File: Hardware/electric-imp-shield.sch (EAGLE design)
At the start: 37 parts, among them Q2 BSS138, Q3 BSS138, U1 ELECTRIC_IMP, U2 ARDUINO_SHIELD, U3 MIC5219-3.3, U4 ATSHA204-TSU

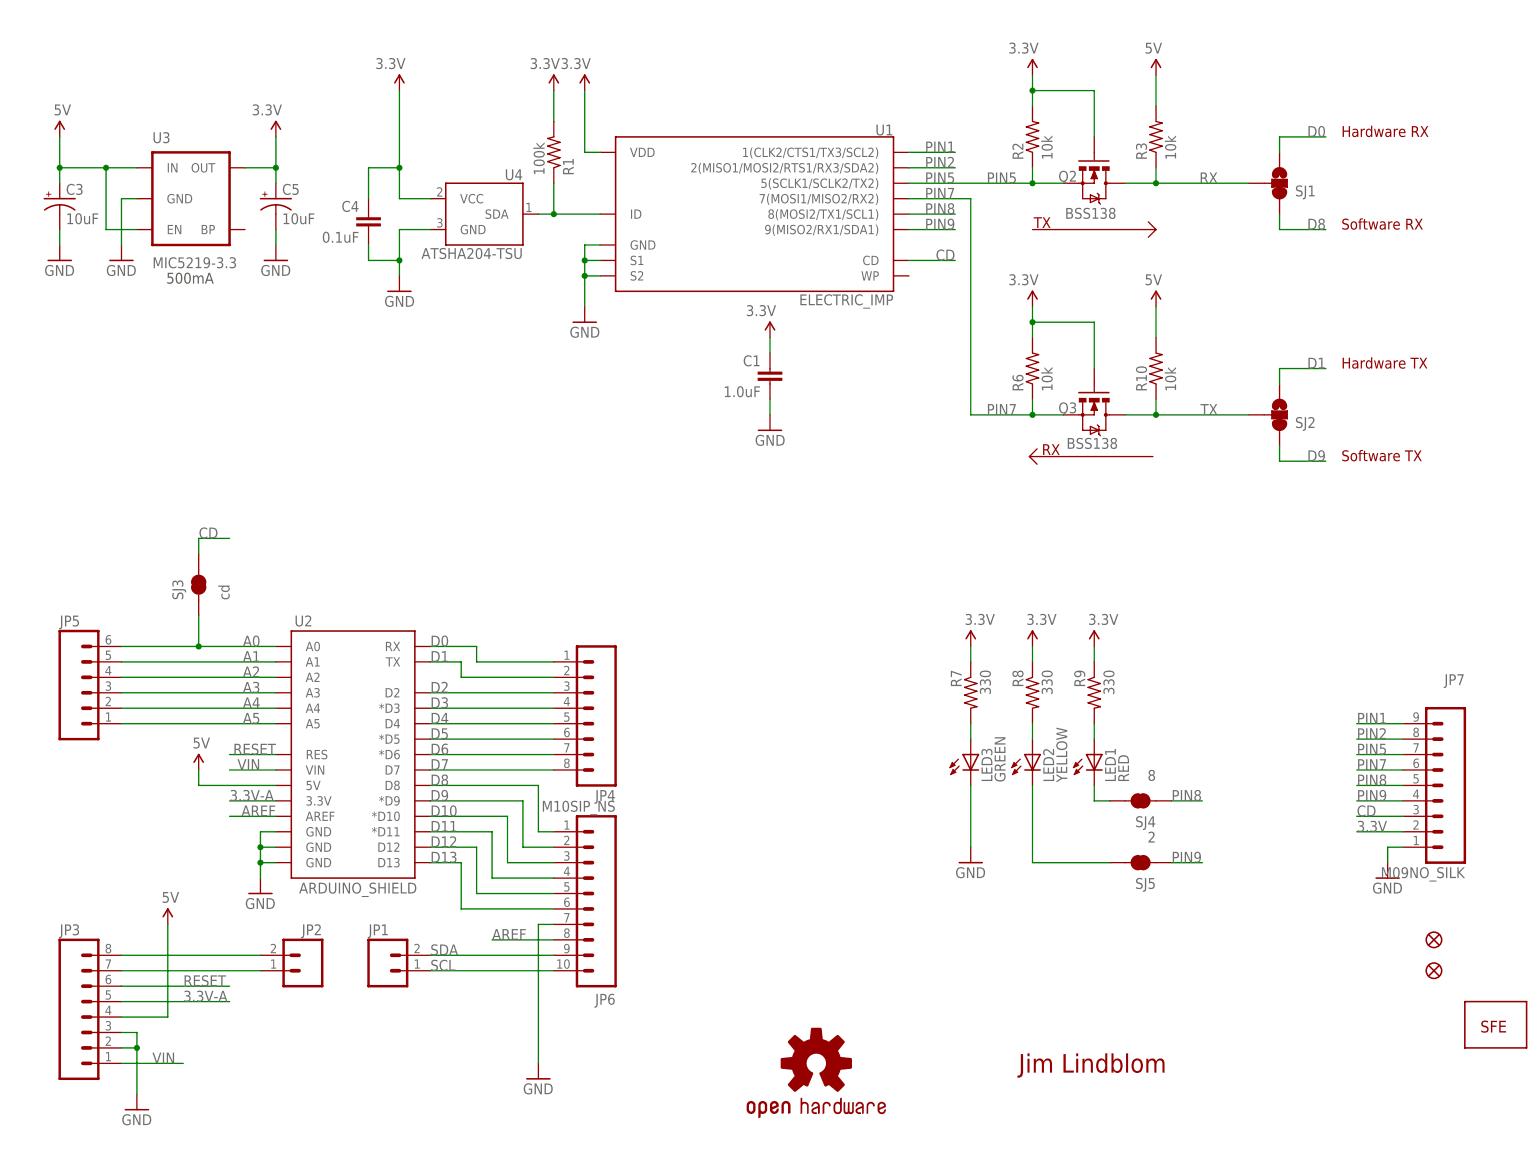
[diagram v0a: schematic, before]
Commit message: Updating to new socket fp, 0603 packages, schematic updates
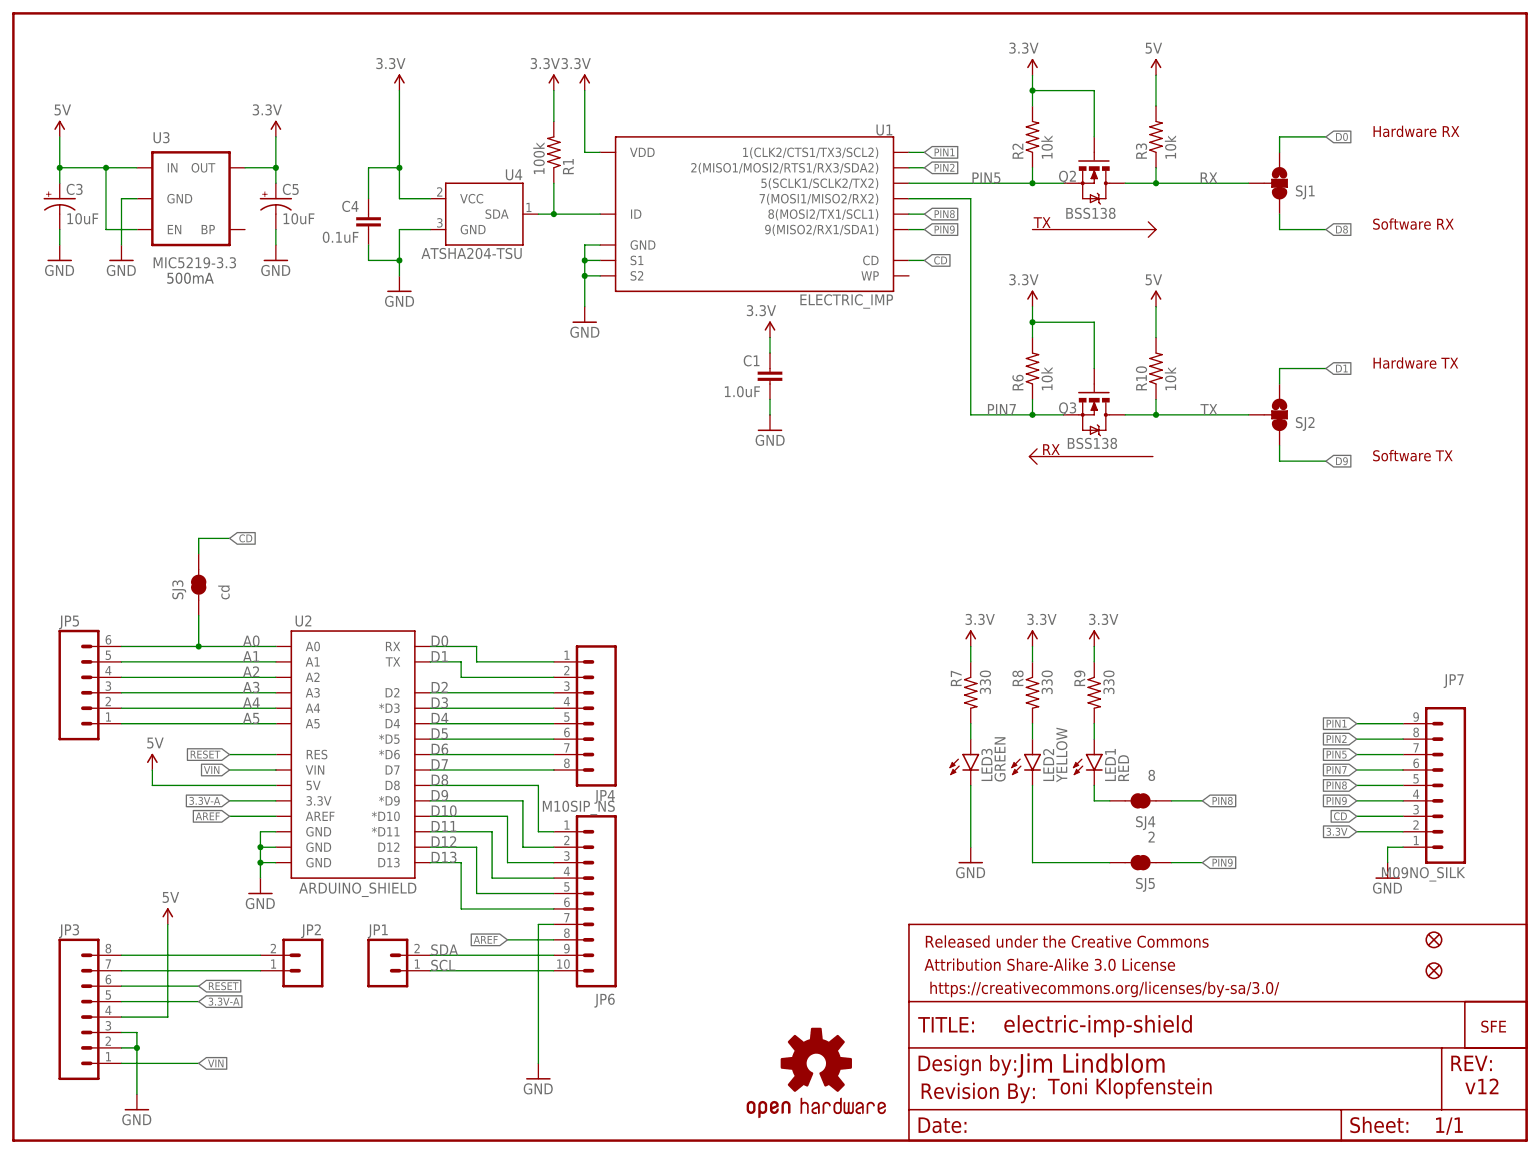
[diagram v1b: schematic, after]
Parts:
- added FRAME1: FRAME-LETTER, SparkFun-Retired:FRAME-LETTER
- added U$6: REVISION, SparkFun-Aesthetics:REVISION
- C1: device SparkFun-Passives:CAP0402-CAP -> SparkFun-Capacitors:1.0UF-16V-10%(0603)
- C3, C5: device SparkFun-Passives:CAP_POL1206 -> SparkFun-Capacitors:10UF-16V-10%(TANT)
- C4: device SparkFun-Passives:CAP0402-CAP -> SparkFun-Capacitors:0.1UF-25V(+80/-20%)(0603)
- LED1: device SparkFun-LED:LED0603 -> SparkFun-LED:LED-RED0603
- LED2: device SparkFun-LED:LED0603 -> SparkFun-LED:LED-YELLOW0603
- LED3: device SparkFun-LED:LED0603 -> SparkFun-LED:LED-GREEN0603
- R1: device SparkFun-Passives:RESISTOR0402-RES -> SparkFun-Resistors:100KOHM1/10W1%(0603)
- R10, R2, R3, R6: device SparkFun-Passives:RESISTOR0402-RES -> SparkFun-Resistors:10KOHM1/10W1%(0603)0603
- R7, R8, R9: device SparkFun-Passives:RESISTOR0402-RES -> SparkFun-Resistors:330OHM1/10W1%(0603)
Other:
- note added: "Toni Klopfenstein"
- note added: "v12"

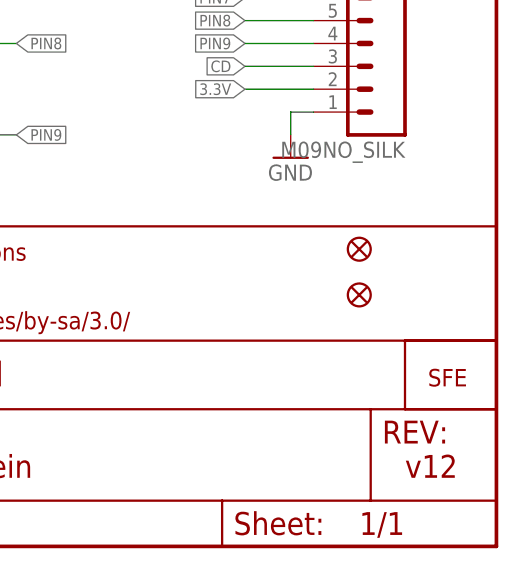
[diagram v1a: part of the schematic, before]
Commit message: removed micro fids, added regulars
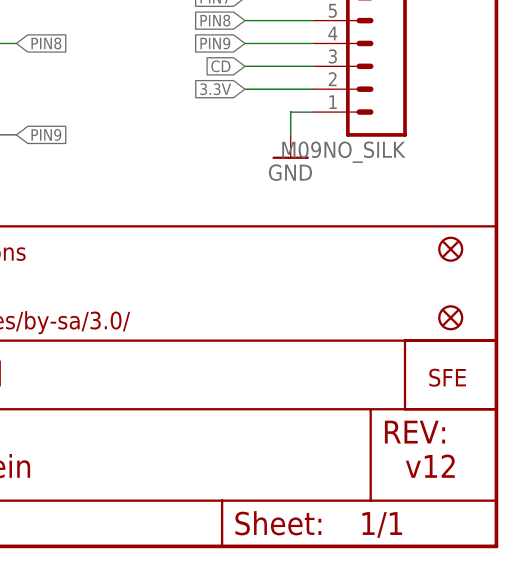
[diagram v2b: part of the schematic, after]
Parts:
- removed JP8, JP9: FIDUCIALUFIDUCIAL, SparkFun:FIDUCIALUFIDUCIAL
- added FID1, FID2: FIDUCIAL1X2, SparkFun-Aesthetics:FIDUCIAL1X2
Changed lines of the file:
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@@
 <?xml version="1.0" encoding="utf-8"?>
 <!DOCTYPE eagle SYSTEM "eagle.dtd">
-<eagle version="6.5.0">
+<eagle version="6.6.0">
 <drawing>
 <settings>
@@
 <part name="JP7" library="SparkFun-Connectors" deviceset="M09" device="NO_SILK"/>
 <part name="GND4" library="SparkFun-Aesthetics" deviceset="GND" device=""/>
-<part name="JP8" library="SparkFun" deviceset="FIDUCIAL" device="UFIDUCIAL"/>
-<part name="JP9" library="SparkFun" deviceset="FIDUCIAL" device="UFIDUCIAL"/>
 <part name="U$6" library="SparkFun-Aesthetics" deviceset="REVISION" device=""/>
+<part name="FID1" library="SparkFun-Aesthetics" deviceset="FIDUCIAL" device="1X2"/>
+<part name="FID2" library="SparkFun-Aesthetics" deviceset="FIDUCIAL" device="1X2"/>
 </parts>
 <sheets>
@@
 <instance part="JP7" gate="G$1" x="238.76" y="58.42" rot="MR0"/>
 <instance part="GND4" gate="1" x="226.06" y="43.18"/>
-<instance part="JP8" gate="G$1" x="233.68" y="33.02"/>
-<instance part="JP9" gate="G$1" x="233.68" y="27.94"/>
 <instance part="U$6" gate="G$1" x="149.098" y="6.858"/>
+<instance part="FID1" gate="G$1" x="243.84" y="33.02"/>
+<instance part="FID2" gate="G$1" x="243.84" y="25.4"/>
 </instances>
 <busses>
